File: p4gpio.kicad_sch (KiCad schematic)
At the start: 38 parts, among them J1 C2760486, J10 Conn_01x04_Socket, J11 Conn_01x04, J2 C2760486, J3 Conn_01x08_Pin, J4 Conn_01x08_Pin, J5 Conn_01x08_Pin, J6 Conn_01x08_Pin, J7 Conn_01x08_Pin, J8 Conn_01x08_Pin, J9 Conn_01x04_Socket, U4 TLV62569DBV

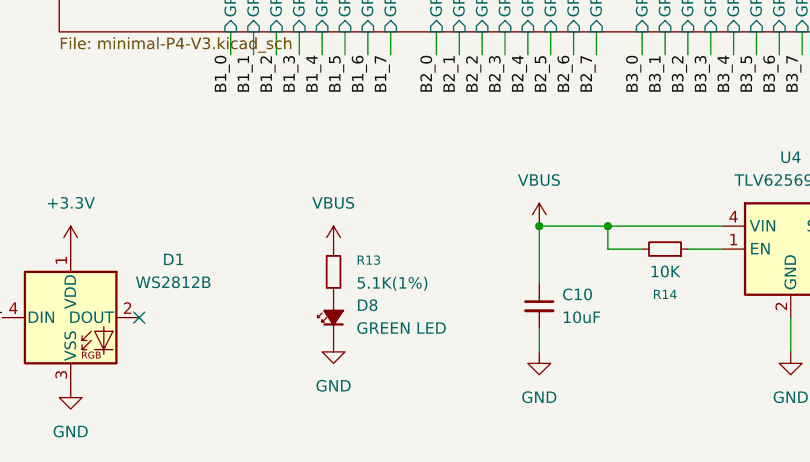
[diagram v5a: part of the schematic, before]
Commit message: Prep to order. Need to make vias bigger
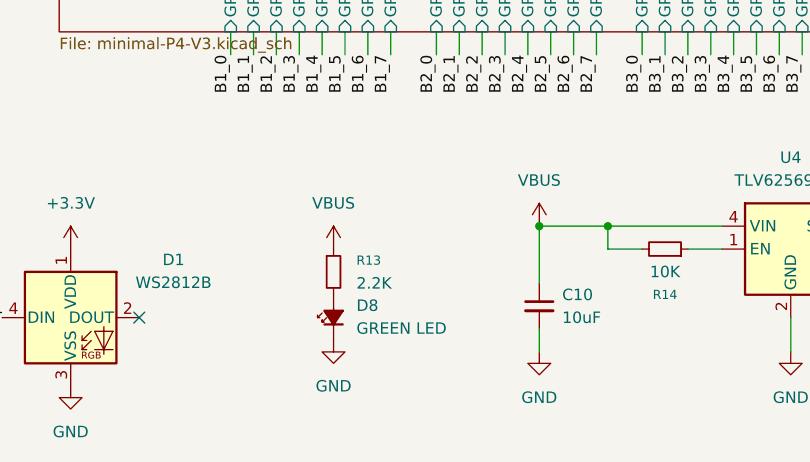
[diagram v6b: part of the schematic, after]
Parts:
- R13: value 5.1K(1%) -> 2.2K
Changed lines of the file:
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@@
 			)
 		)
-		(property "Value" "5.1K(1%)"
+		(property "Value" "2.2K"
 			(at 71.12 168.9099 0)
 			(show_name no)

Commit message: Connect flash VDD and skooch USBs apart. Start of v2
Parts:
- J1, J2: footprint Connector_USB:USB_C_Receptacle_HRO_TYPE-C-31-M-12 -> Adafruit:USB_C_Receptacle_HRO_TYPE-C-31-M-31
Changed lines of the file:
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@@
 			)
 		)
-		(property "Footprint" "Connector_USB:USB_C_Receptacle_HRO_TYPE-C-31-M-12"
+		(property "Footprint" "Adafruit:USB_C_Receptacle_HRO_TYPE-C-31-M-31"
 			(at 236.22 33.02 0)
 			(hide yes)
@@
 			)
 		)
-		(property "Footprint" "Connector_USB:USB_C_Receptacle_HRO_TYPE-C-31-M-12"
+		(property "Footprint" "Adafruit:USB_C_Receptacle_HRO_TYPE-C-31-M-31"
 			(at 167.64 33.02 0)
 			(hide yes)

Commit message: ready for v2
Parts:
- R13: value 2.2K -> 5.1K(1%)
- R14, R209, R210: value 10K -> 10K(1%)
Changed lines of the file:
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@@
 			)
 		)
-		(property "Value" "10K"
+		(property "Value" "10K(1%)"
 			(at 167.386 134.112 0)
 			(show_name no)
@@
 			)
 		)
-		(property "Value" "10K"
+		(property "Value" "10K(1%)"
 			(at 161.798 130.81 0)
 			(show_name no)
@@
 			)
 		)
-		(property "Value" "2.2K"
+		(property "Value" "5.1K(1%)"
 			(at 71.12 168.9099 0)
 			(show_name no)
@@
 			)
 		)
-		(property "Value" "10K"
+		(property "Value" "10K(1%)"
 			(at 105.41 167.64 90)
 			(show_name no)
